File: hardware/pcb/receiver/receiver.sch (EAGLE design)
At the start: 18 parts, among them X1 SMA-142-0701-801/806

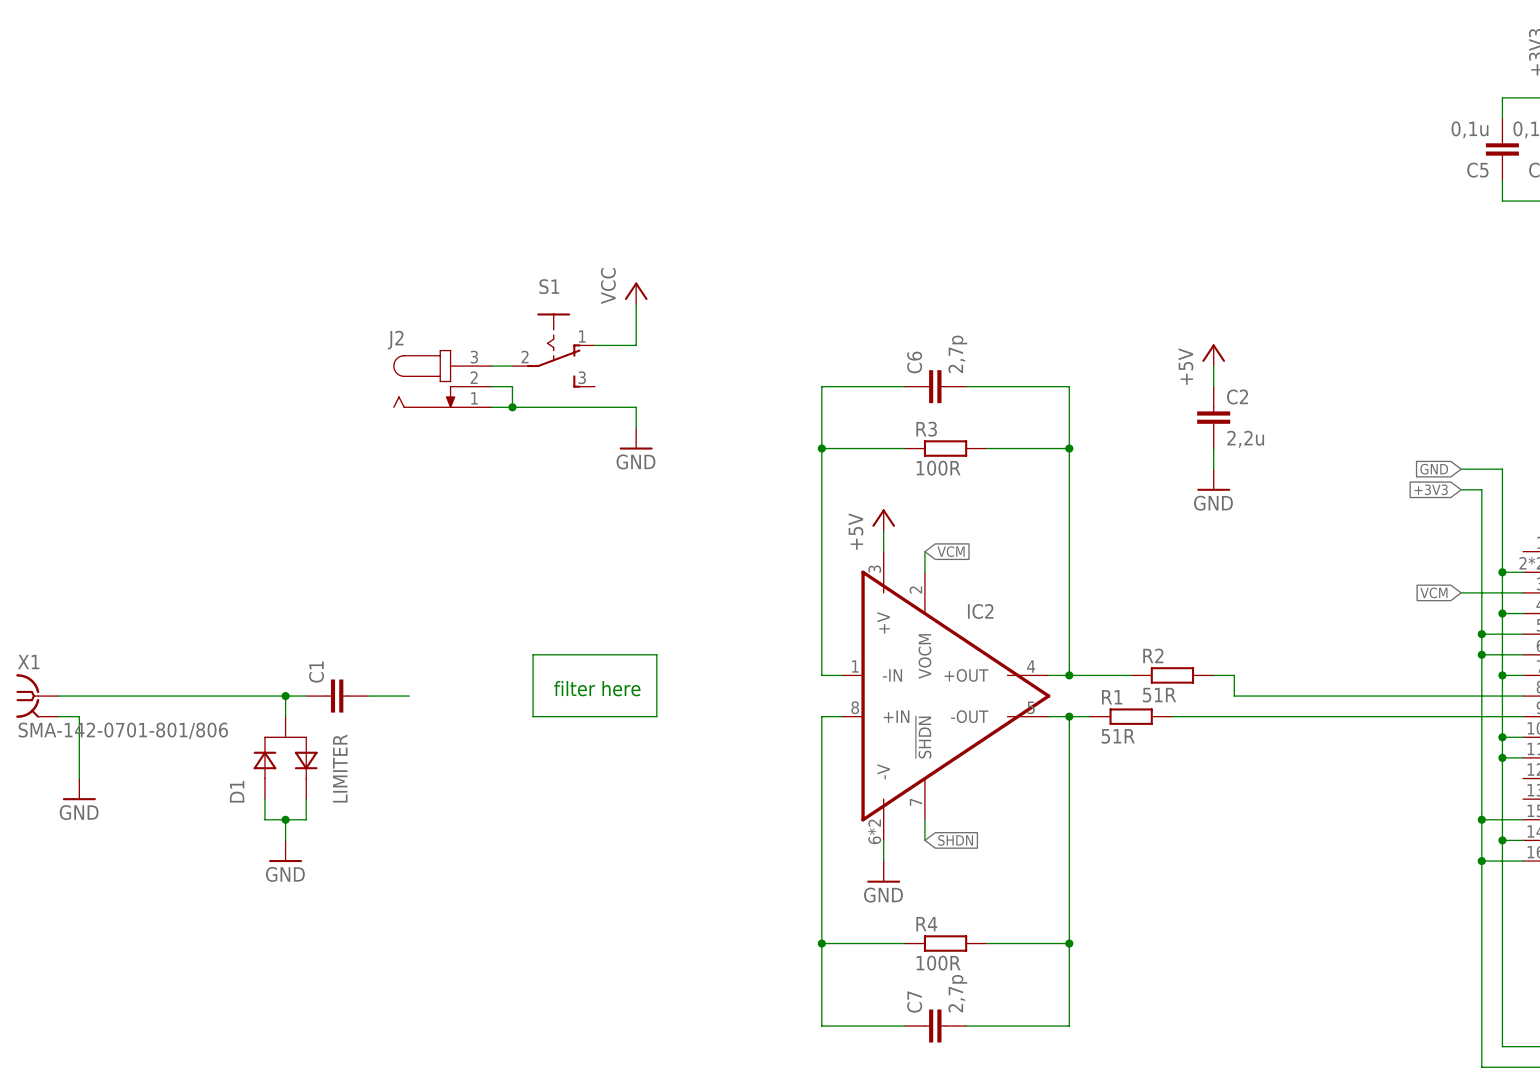
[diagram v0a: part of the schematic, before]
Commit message: hw: misc changes, added fuses to power supply units
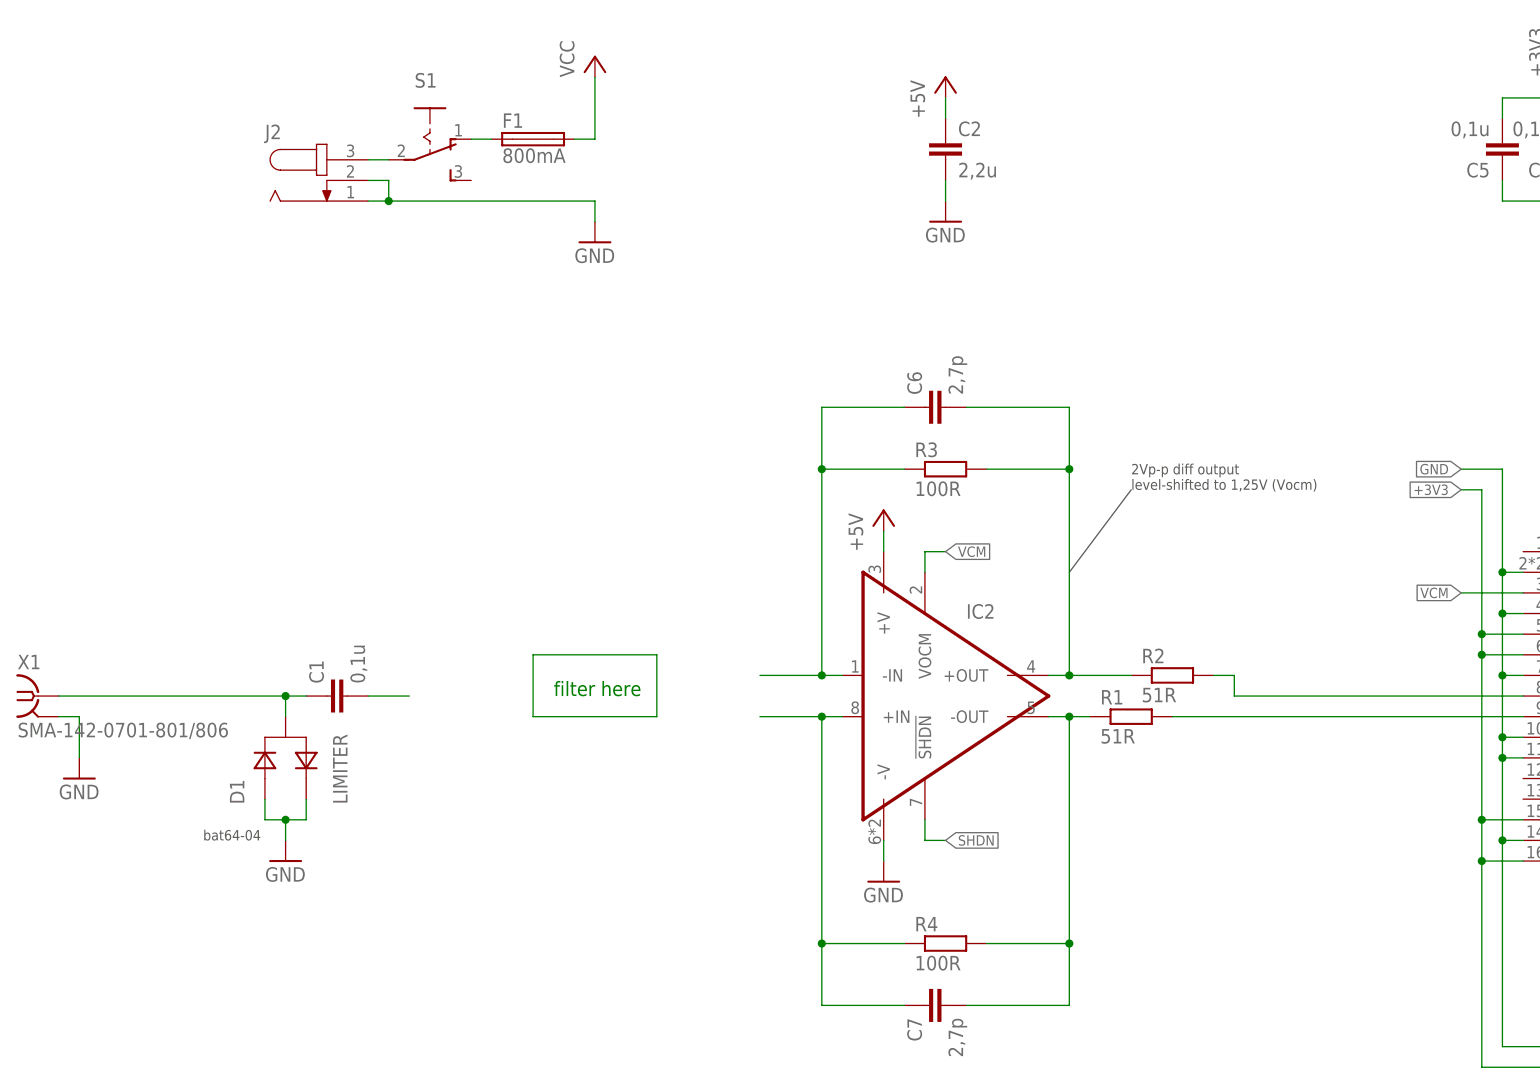
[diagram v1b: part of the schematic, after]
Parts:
- added F1: 800mA, fuse:GSH15
- C1: value (none) -> 0,1u
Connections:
- new net N$13: F1.1, S1.O
- net VCC: now also F1.2; no longer S1.O
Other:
- note added: "2Vp-p diff output level-shifted to 1,25V (Vocm)"
- note added: "bat64-04"
- moved on the sheet: C2, C6, C7, J2, R3, S1

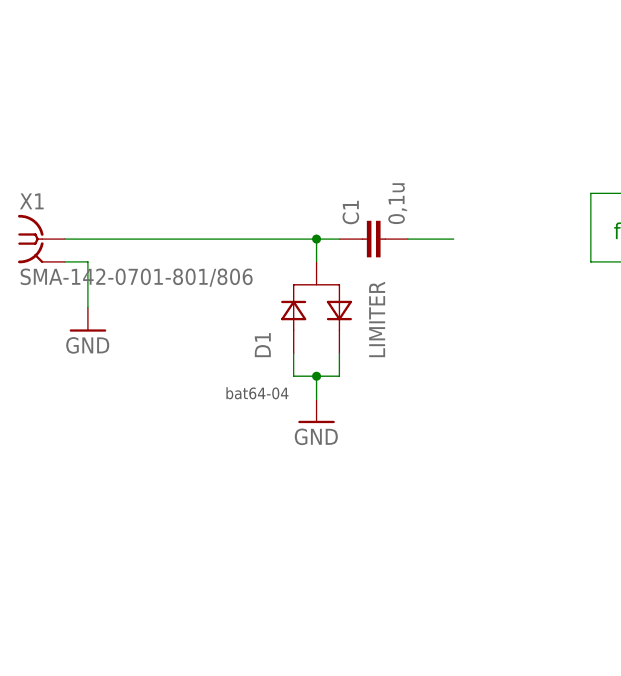
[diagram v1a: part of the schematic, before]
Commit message: hw: added n2adr sdr circuit as an example hw: added tvs diode to receiver
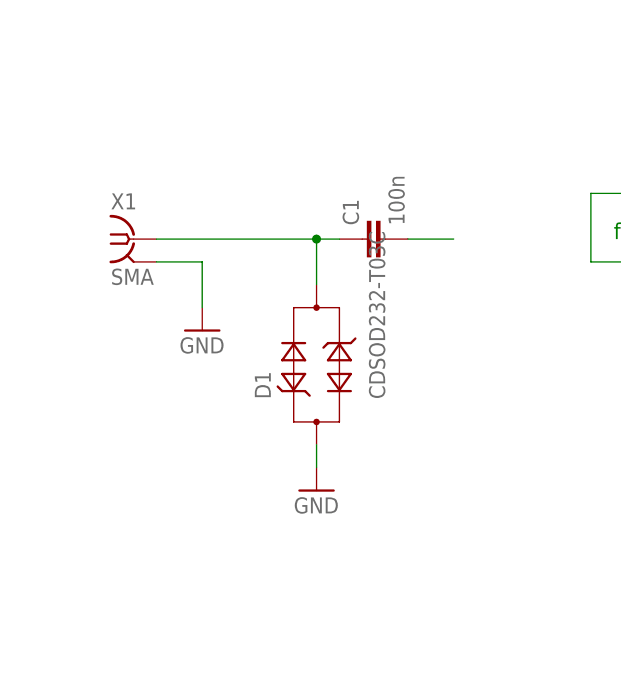
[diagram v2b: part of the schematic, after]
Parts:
- C1: value 0,1u -> 100n
- D1: value LIMITER -> CDSOD232-T03C; device lstolcman_thesis:LIMITER -> lstolcman_thesis:CDSOD232
- X1: value SMA-142-0701-801/806 -> SMA
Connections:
- net GND: no longer D1.1
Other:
- note removed: "bat64-04"
- moved on the sheet: X1
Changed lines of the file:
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@@
 <setting verticaltext="up"/>
 </settings>
-<grid distance="0.1" unitdist="inch" unit="mil" style="lines" multiple="1" display="yes" altdistance="0.01" altunitdist="inch" altunit="mil"/>
+<grid distance="0.1" unitdist="inch" unit="inch" style="lines" multiple="1" display="yes" altdistance="0.01" altunitdist="inch" altunit="inch"/>
 <layers>
 <layer number="1" name="Top" color="4" fill="1" visible="no" active="no"/>
@@
 </classes>
 <parts>
-<part name="X1" library="con-coax" deviceset="SMA-" device="142-0701-801/806"/>
+<part name="X1" library="con-coax" deviceset="SMA-" device="142-0701-801/806" value="SMA"/>
 <part name="GND1" library="supply1" deviceset="GND" device=""/>
 <part name="GND2" library="supply1" deviceset="GND" device=""/>
-<part name="C1" library="rcl" deviceset="C-EU" device="C0805" value="0,1u"/>
+<part name="C1" library="rcl" deviceset="C-EU" device="C0805" value="100n"/>
 <part name="GND3" library="supply1" deviceset="GND" device=""/>
 <part name="J2" library="con-jack" deviceset="JACK-PLUG" device="0"/>
@@
 <part name="SV1" library="lstolcman_thesis" deviceset="PINHEADER" device=""/>
 <part name="IC2" library="lstolcman_thesis" deviceset="LTC6405" device=""/>
-<part name="D1" library="lstolcman_thesis" deviceset="LIMITER" device=""/>
 <part name="C2" library="rcl" deviceset="C-EU" device="C0805" value="2,2u"/>
 <part name="GND5" library="supply1" deviceset="GND" device=""/>
@@
 <part name="C7" library="rcl" deviceset="C-EU" device="C0805" value="2,7p"/>
 <part name="F1" library="fuse" deviceset="GSH15" device="" value="800mA"/>
+<part name="D1" library="lstolcman_thesis" deviceset="CDSOD232" device="" value="CDSOD232-T03C"/>
 </parts>
 <sheets>
@@
 level-shifted to 1,25V (Vocm)</text>
 <wire x1="109.22" y1="66.04" x2="101.6" y2="55.88" width="0.0508" layer="97"/>
-<text x="-5.08" y="22.86" size="1.27" layer="97">bat64-04</text>
 </plain>
 <instances>
-<instance part="X1" gate="G1" x="-25.4" y="40.64"/>
-<instance part="GND1" gate="1" x="5.08" y="20.32"/>
-<instance part="GND2" gate="1" x="-20.32" y="30.48"/>
+<instance part="X1" gate="G1" x="-15.24" y="40.64"/>
+<instance part="GND1" gate="1" x="5.08" y="12.7"/>
+<instance part="GND2" gate="1" x="-7.62" y="30.48"/>
 <instance part="C1" gate="G$1" x="10.16" y="40.64" rot="R90"/>
 <instance part="GND3" gate="1" x="43.18" y="96.52"/>
@@
 <instance part="SV1" gate="G$1" x="294.64" y="33.02"/>
 <instance part="IC2" gate="G$1" x="81.28" y="40.64"/>
-<instance part="D1" gate="G$1" x="10.16" y="33.02"/>
 <instance part="C2" gate="G$1" x="86.36" y="109.22"/>
 <instance part="GND5" gate="1" x="86.36" y="99.06"/>
@@
 <instance part="C7" gate="G$1" x="83.82" y="2.54" rot="MR270"/>
 <instance part="F1" gate="1" x="35.56" y="109.22"/>
+<instance part="D1" gate="G$1" x="5.08" y="27.94" rot="R90"/>
 </instances>
 <busses>
@@
 <net name="GND" class="0">
 <segment>
-<wire x1="7.62" y1="27.94" x2="7.62" y2="25.4" width="0.1524" layer="91"/>
-<wire x1="7.62" y1="25.4" x2="5.08" y2="25.4" width="0.1524" layer="91"/>
-<wire x1="5.08" y1="25.4" x2="2.54" y2="25.4" width="0.1524" layer="91"/>
-<wire x1="2.54" y1="25.4" x2="2.54" y2="27.94" width="0.1524" layer="91"/>
-<wire x1="5.08" y1="25.4" x2="5.08" y2="22.86" width="0.1524" layer="91"/>
-<junction x="5.08" y="25.4"/>
-<pinref part="GND1" gate="1" pin="GND"/>
-<pinref part="D1" gate="G$1" pin="1"/>
-<pinref part="D1" gate="G$1" pin="2"/>
-</segment>
-<segment>
 <pinref part="X1" gate="G1" pin="2"/>
-<wire x1="-22.86" y1="38.1" x2="-20.32" y2="38.1" width="0.1524" layer="91"/>
-<wire x1="-20.32" y1="38.1" x2="-20.32" y2="33.02" width="0.1524" layer="91"/>
+<wire x1="-12.7" y1="38.1" x2="-7.62" y2="38.1" width="0.1524" layer="91"/>
+<wire x1="-7.62" y1="38.1" x2="-7.62" y2="33.02" width="0.1524" layer="91"/>
 <pinref part="GND2" gate="1" pin="GND"/>
 </segment>
@@
 <wire x1="162.56" y1="101.6" x2="162.56" y2="104.14" width="0.1524" layer="91"/>
 </segment>
+<segment>
+<pinref part="GND1" gate="1" pin="GND"/>
+<wire x1="5.08" y1="15.24" x2="5.08" y2="17.78" width="0.1524" layer="91"/>
+<pinref part="D1" gate="G$1" pin="2"/>
+</segment>
 </net>
 <net name="N$2" class="0">
 <segment>
 <pinref part="X1" gate="G1" pin="1"/>
-<wire x1="-22.86" y1="40.64" x2="5.08" y2="40.64" width="0.1524" layer="91"/>
-<wire x1="5.08" y1="40.64" x2="5.08" y2="38.1" width="0.1524" layer="91"/>
+<wire x1="-12.7" y1="40.64" x2="5.08" y2="40.64" width="0.1524" layer="91"/>
+<wire x1="5.08" y1="40.64" x2="5.08" y2="35.56" width="0.1524" layer="91"/>
 <pinref part="C1" gate="G$1" pin="1"/>
 <wire x1="5.08" y1="40.64" x2="7.62" y2="40.64" width="0.1524" layer="91"/>

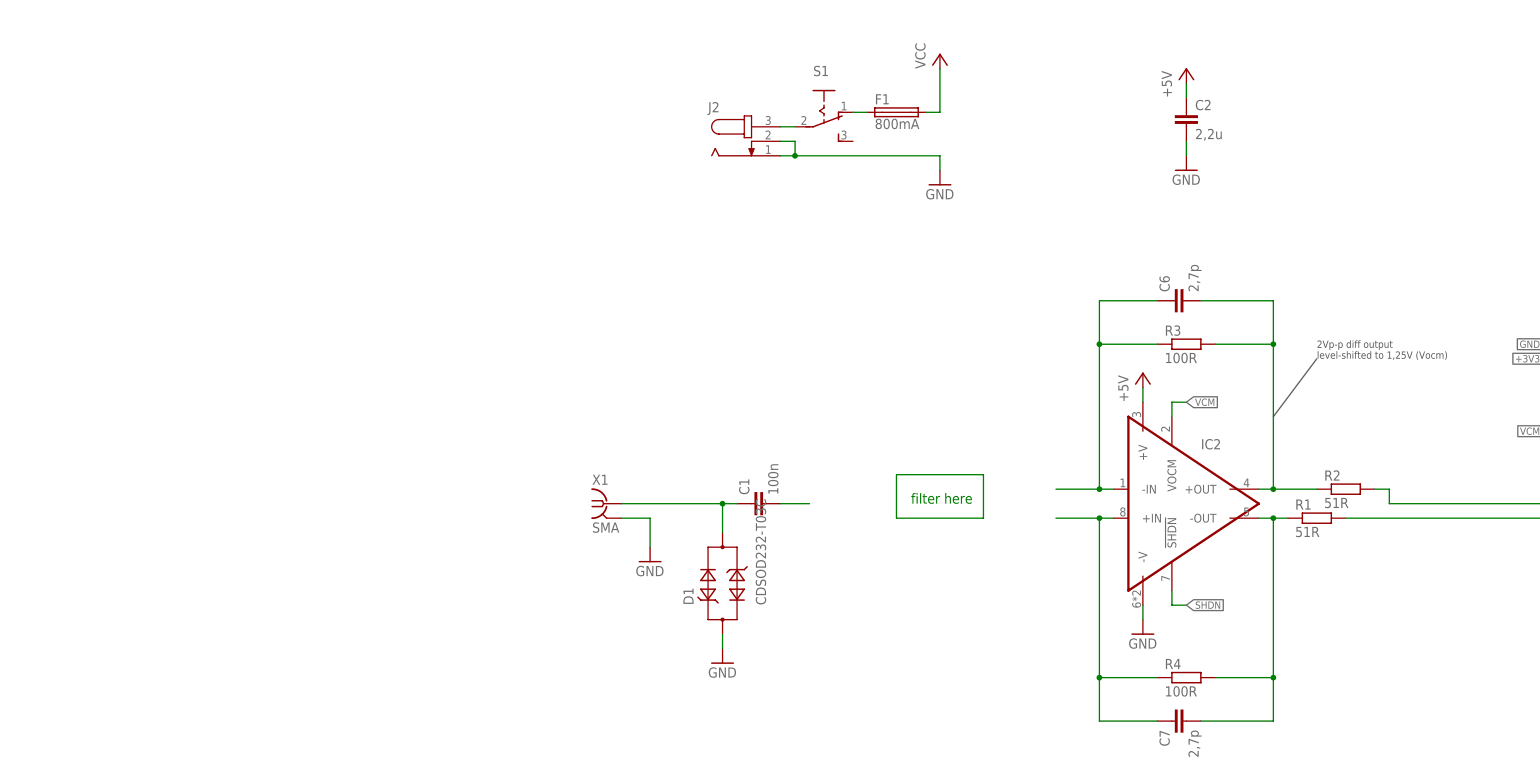
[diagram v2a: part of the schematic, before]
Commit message: hw: receiver power supply
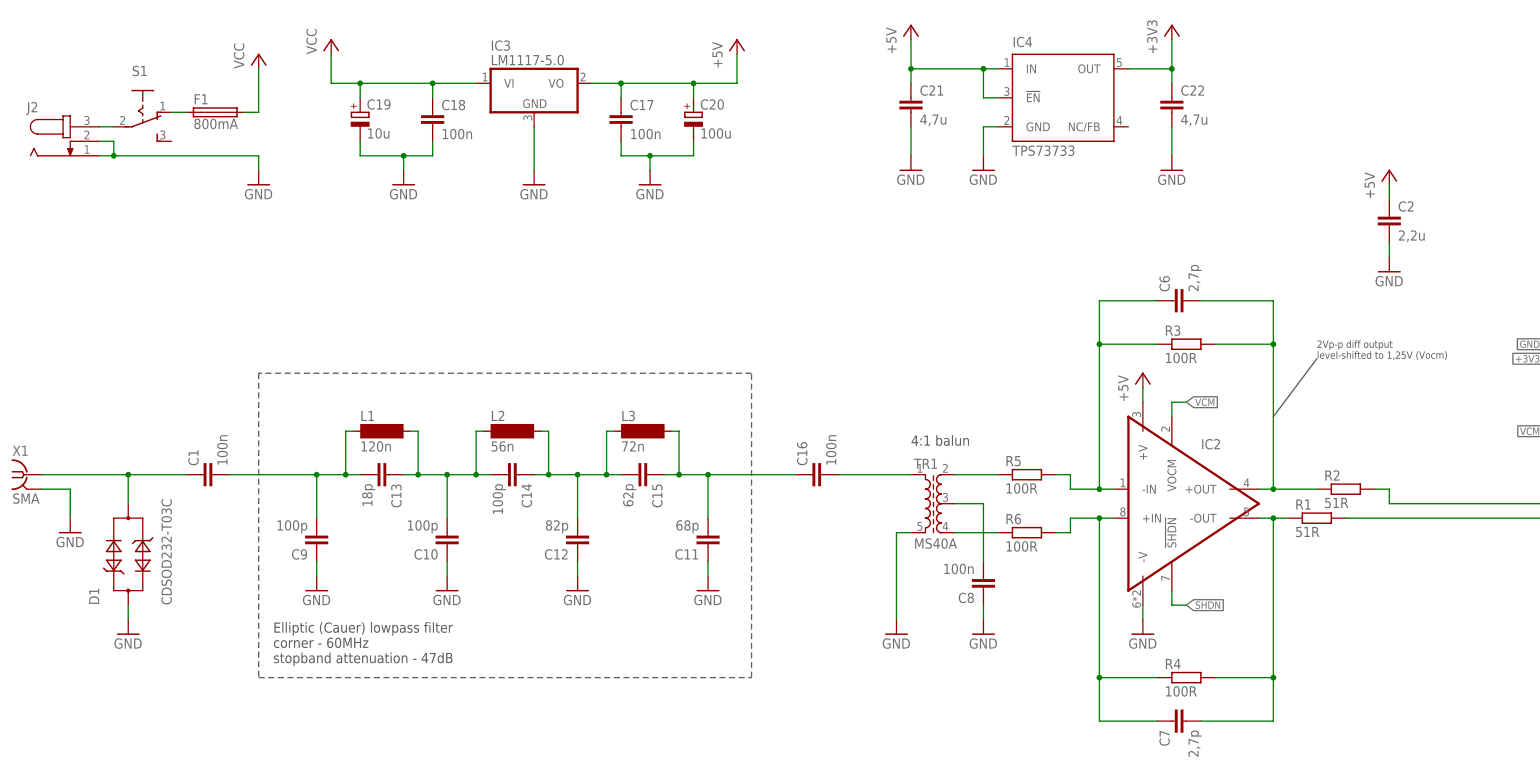
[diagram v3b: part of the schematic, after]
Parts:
- added C10, C14, C9: 100p, rcl:C-EUC0805
- added C11: 68p, rcl:C-EUC0805
- added C12: 82p, rcl:C-EUC0805
- added C13: 18p, rcl:C-EUC0805
- added C15: 62p, rcl:C-EUC0805
- added C16, C17, C18, C8: 100n, rcl:C-EUC0805
- added C19: 10u, rcl:CPOL-EUC
- added C20: 100u, rcl:CPOL-EUC
- added C21, C22: 4,7u, rcl:C-EUC0805
- added IC3: LM1117-5.0, linear:7806DT
- added IC4: TPS73733, texas:TPS77001
- added L1: 120n, inductor-neosid:SM-NE29
- added L2: 56n, inductor-neosid:SM-NE29
- added L3: 72n, inductor-neosid:SM-NE29
- added R5, R6: 100R, rcl:R-EU_M1206
- added TR1: MS40A, inductor-neosid:MS40A
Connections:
- new net N$14: R6.1, TR1.4
- new net N$15: C8.2, TR1.3
- new net N$16: C1.2, C13.2, C9.2, L1.1
- new net N$17: C10.2, C13.1, C14.2, L1.2, L2.1
- new net N$18: C12.2, C14.1, C15.2, L2.2, L3.1
- new net N$19: C11.2, C15.1, C16.1, L3.2
- new net N$3: C16.2, TR1.1
- net +3V3: now also C22.1, IC4.OUT
- net +5V: now also C17.1, C20.+, C21.1, IC3.VO, IC4.!EN, IC4.IN
- net GND: now also C10.1, C11.1, C12.1, C17.2, C18.2, C19.-, C20.-, C21.2, C22.2, C8.1, C9.1, IC3.GND, IC4.GND, TR1.5
- net N$1: now also R5.1, TR1.2; no longer C1.2
- net N$4: now also R5.2
- net N$5: now also R6.2
- net VCC: now also C18.1, C19.+, IC3.VI
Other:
- note added: "4:1 balun"
- note added: "Elliptic (Cauer) lowpass filter corner - 60MHz stopband attenuation - 47dB"
- note removed: "filter here"
- moved on the sheet: C1, C2, D1, F1, J2, S1, X1
